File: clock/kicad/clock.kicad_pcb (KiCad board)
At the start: 2 copper layers, 152.9 x 74.9 mm, 79 parts, among them J1 USB-SS-52100-001, Q1 PN2222A, SW1 HOUR, SW2 MIN, SW3 TIME, U1 74HC4060, U10 74HC390, U11 NE555P, U12 74HC4511, U13 74HC4511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

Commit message: Clock: Added missing pulldown resistor to Time button.
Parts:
- added R7: 100K, Resistor_THT:R_Axial_DIN0207_L6.3mm_D2.5mm_P7.62mm_Horizontal, F.Cu at (223.4, 92.8)
- renumbered R9 to R10, R10 to R11, R11 to R12, R7 to R8, R8 to R9
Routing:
- net Net-(R7-Pad2): track 75.7 -> 80.7 mm

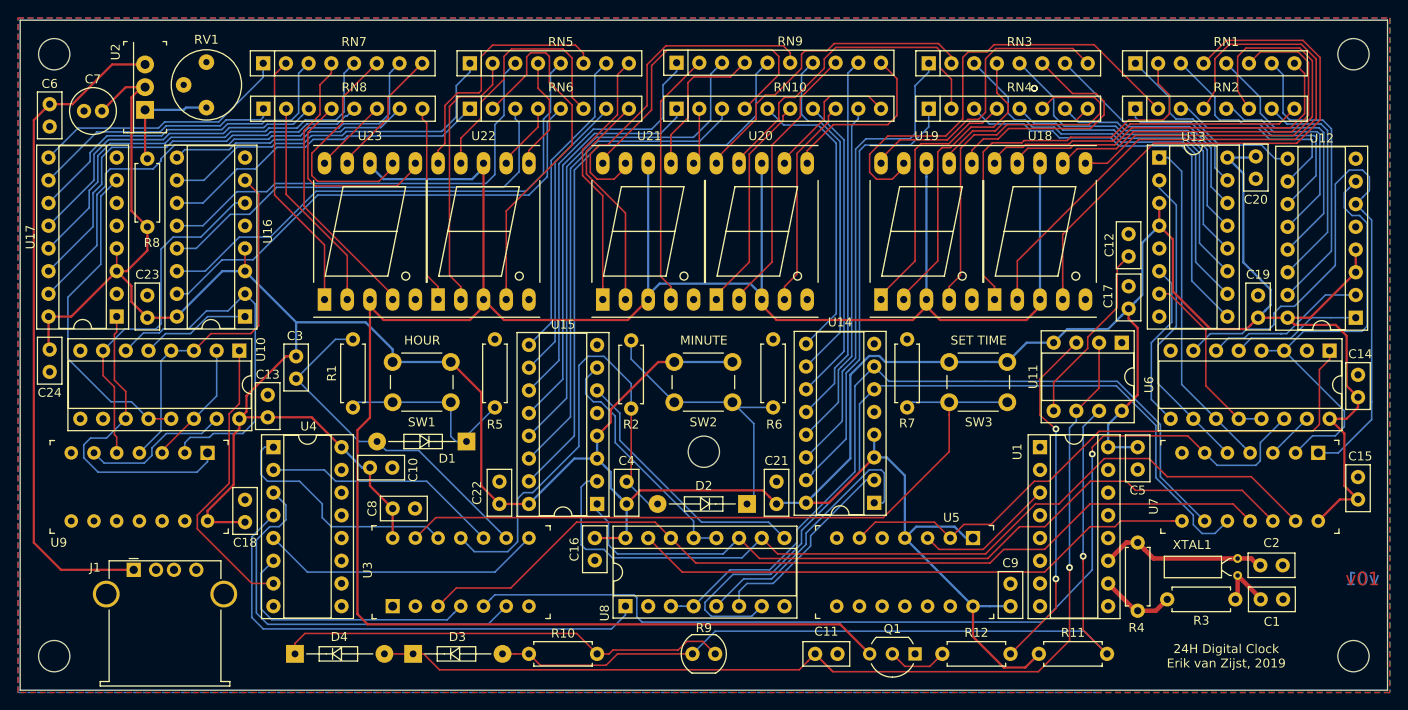
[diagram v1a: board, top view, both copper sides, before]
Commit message: Clock: Time Switch Resets Seconds.
Added a two-diode OR gate to use the Time switch as a secondary input
for the seconds counter's reset lines.
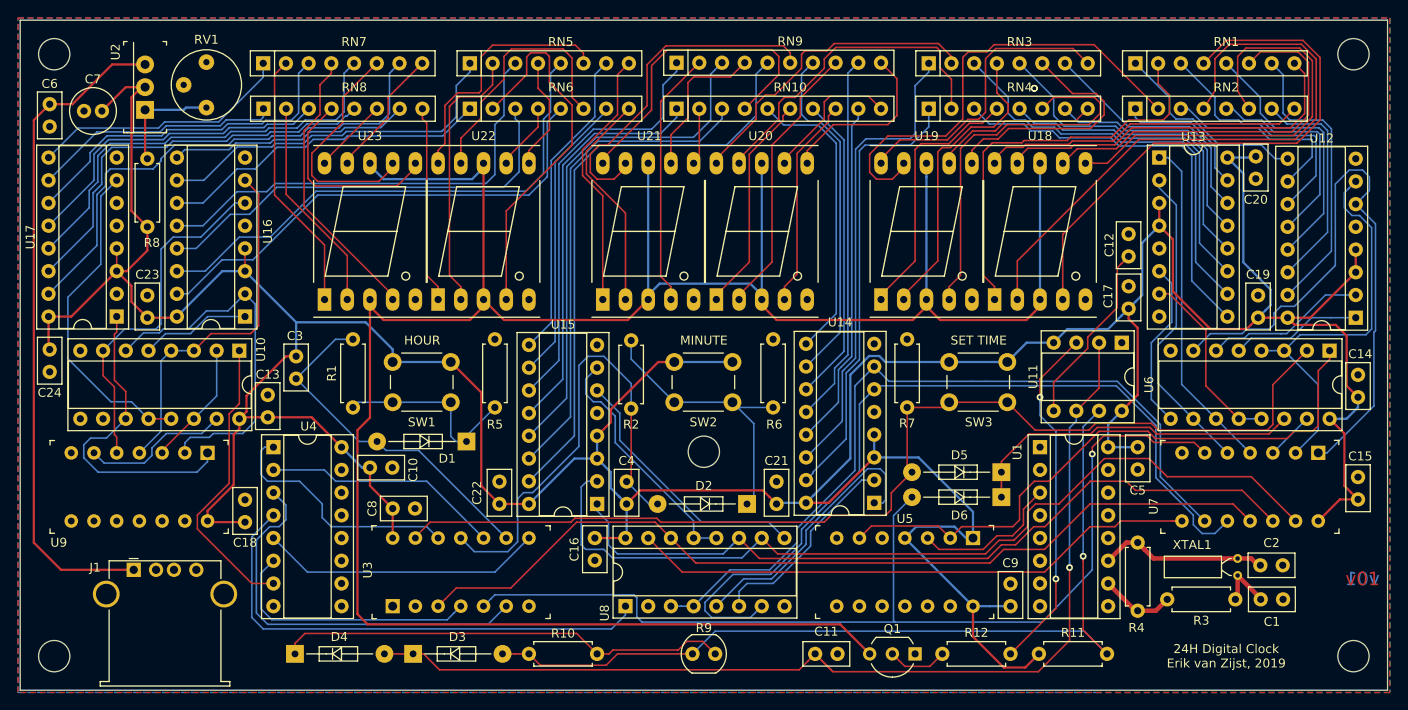
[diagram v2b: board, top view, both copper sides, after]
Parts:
- added D5: D, digikey-footprints:Diode_DO-35_P10mm, F.Cu at (233.9, 107.7)
- added D6: D, digikey-footprints:Diode_DO-35_P10mm, F.Cu at (233.9, 110.5)
- R10: value 1M -> 470K
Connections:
- R7 pad 2: Net-(R7-Pad2) -> Net-(D5-Pad2)
- SW3 pad 2: Net-(R7-Pad2) -> Net-(D5-Pad2)
- U3 pad 13: Net-(R7-Pad2) -> Net-(D5-Pad2)
- U3 pad 5: Net-(U3-Pad5) -> Net-(D6-Pad2)
- U6 pad 14: Net-(U3-Pad5) -> Net-(D5-Pad1)
- U6 pad 2: GND -> Net-(D5-Pad2)
- U7 pad 6: Net-(U3-Pad5) -> Net-(D6-Pad2)
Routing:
- net Net-(D5-Pad2): track 0.00 -> 120.7 mm
- net Net-(D6-Pad2): track 0.00 -> 116.1 mm, vias 0 -> 1
- net Net-(U3-Pad5): track 114.0 -> 0.00 mm, vias 1 -> 0
- net Net-(R7-Pad2): track 80.7 -> 0.00 mm
- net Net-(D5-Pad1): track 0.00 -> 38.2 mm
- net VCC: track 481.3 -> 486.5 mm
- net Net-(U12-Pad7): track 49.2 -> 46.2 mm
- net Net-(U5-Pad2): track 66.9 -> 68.8 mm
- net Net-(U1-Pad3): track 15.7 -> 16.7 mm
- net Net-(U15-Pad2): track 98.0 -> 98.9 mm

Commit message: Clock: Switched 24H counter's high digit to quinary counter to match breadboard version.
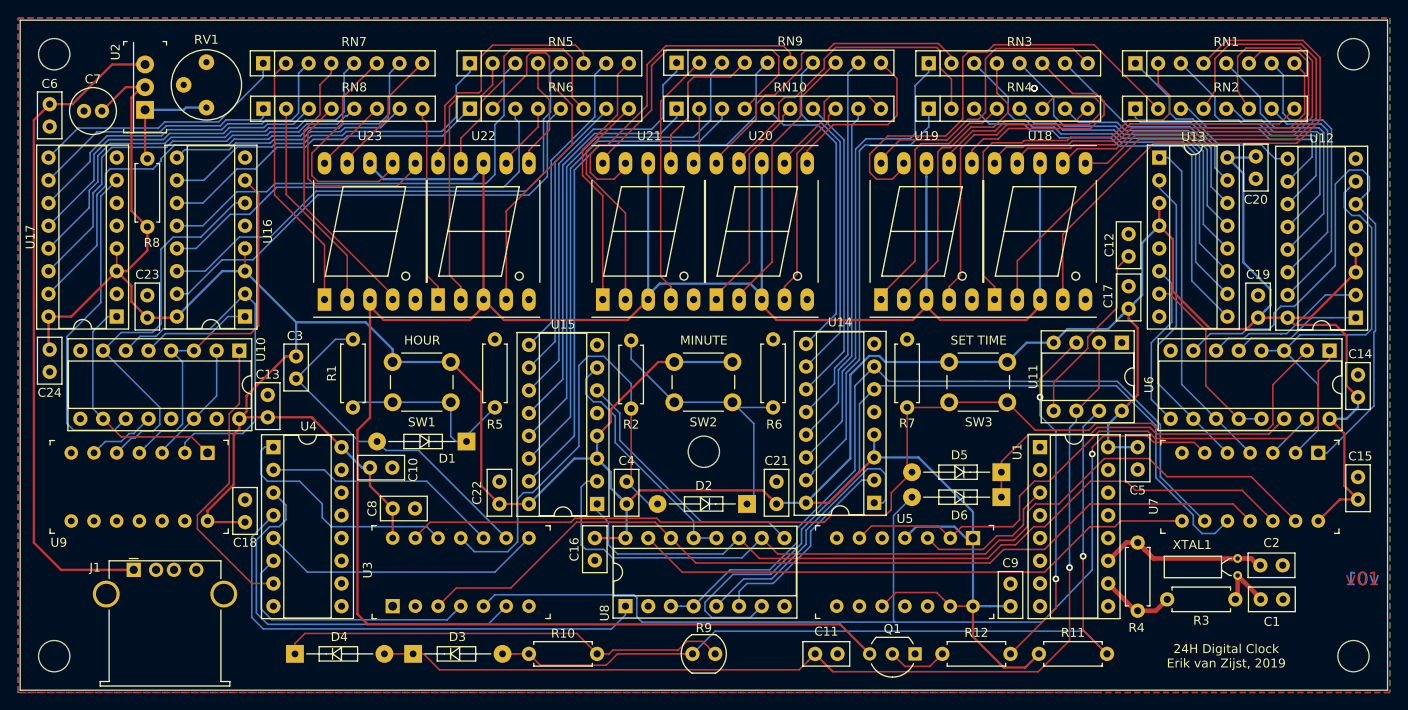
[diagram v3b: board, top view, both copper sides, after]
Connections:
- U10 pad 13: Net-(U10-Pad12) -> Net-(U10-Pad13)
- U10 pad 15: Net-(U10-Pad15) -> GND
- U17 pad 1: Net-(U10-Pad11) -> Net-(U10-Pad10)
- U17 pad 7: Net-(U10-Pad12) -> Net-(U10-Pad11)
- U18 pad 5: Net-(U18-Pad5) -> GND
- U19 pad 5: Net-(U19-Pad5) -> GND
- U20 pad 5: Net-(U20-Pad5) -> GND
- U21 pad 5: Net-(U21-Pad5) -> GND
- U22 pad 5: Net-(U22-Pad5) -> GND
- U5 pad 10: Net-(U5-Pad10) -> VCC
- U5 pad 11: Net-(U5-Pad11) -> GND
- U5 pad 12: Net-(U5-Pad12) -> GND
- U5 pad 13: Net-(U5-Pad13) -> VCC
- U9 pad 1: Net-(U10-Pad11) -> Net-(U10-Pad10)
- U9 pad 6: Net-(U10-Pad15) -> Net-(U10-Pad12)
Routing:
- net Net-(U10-Pad12): track 36.5 -> 7.67 mm
- net Net-(U10-Pad10): track 0.00 -> 26.8 mm
- net Net-(U10-Pad15): track 16.7 -> 0.00 mm
- net VCC: track 486.5 -> 494.8 mm
- net Net-(U10-Pad7): track 39.7 -> 44.6 mm
- net Net-(U10-Pad3): track 40.7 -> 42.7 mm
- net Net-(U10-Pad11): track 35.4 -> 36.9 mm
